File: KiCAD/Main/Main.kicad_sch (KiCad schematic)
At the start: 5 parts, among them J5 Conn_02x04_Counter_Clockwise

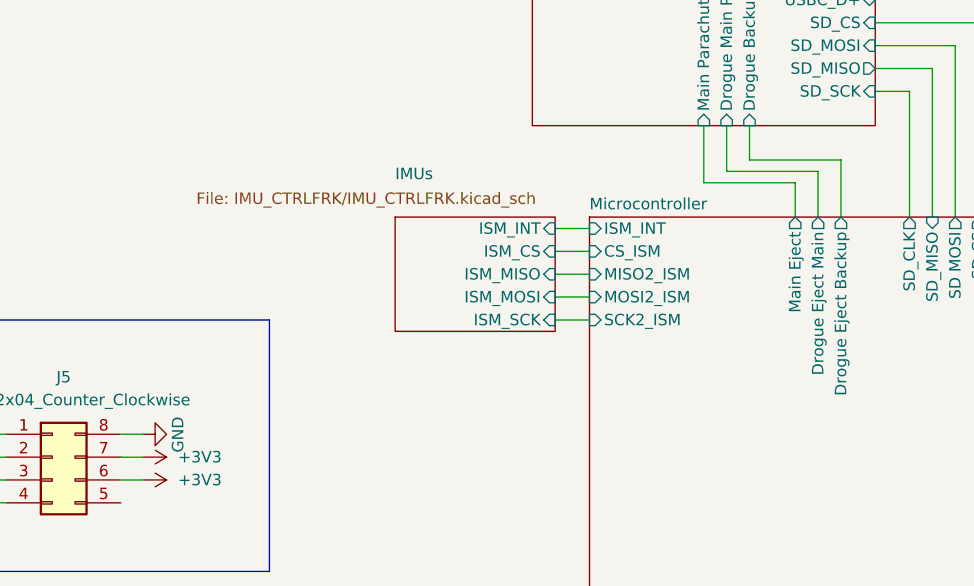
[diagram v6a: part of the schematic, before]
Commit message: Replace independent magnetometer, reformat test points, generate test gerber and BOM
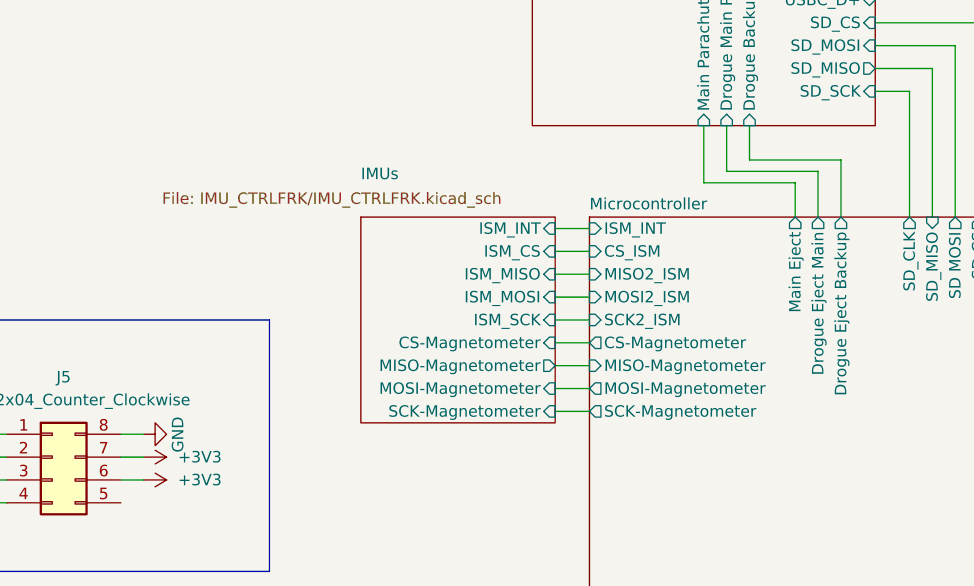
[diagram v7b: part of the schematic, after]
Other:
- sheet IMUs ports: added CS-Magnetometer, MISO-Magnetometer, MOSI-Magnetometer, SCK-Magnetometer; removed none
- sheet Microcontroller ports: added CS-Magnetometer, MISO-Magnetometer, MOSI-Magnetometer, SCK-Magnetometer; removed none
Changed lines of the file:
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@@
+	(wire
+		(pts
+			(xy 102.87 85.09) (xy 106.68 85.09)
+		)
+		(stroke
+			(width 0)
+			(type default)
+		)
+	)
 	(wire
 		(pts
@@
 	(wire
 		(pts
+			(xy 102.87 80.01) (xy 106.68 80.01)
+		)
+		(stroke
+			(width 0)
+			(type default)
+		)
+	)
+	(wire
+		(pts
 			(xy 168.91 113.03) (xy 172.72 113.03)
 		)
@@
 	(wire
 		(pts
+			(xy 102.87 82.55) (xy 106.68 82.55)
+		)
+		(stroke
+			(width 0)
+			(type default)
+		)
+	)
+	(wire
+		(pts
 			(xy 102.87 74.93) (xy 106.68 74.93)
 		)
@@
 		(pts
 			(xy 102.87 140.97) (xy 106.68 140.97)
+		)
+		(stroke
+			(width 0)
+			(type default)
+		)
+	)
+	(wire
+		(pts
+			(xy 102.87 87.63) (xy 106.68 87.63)
 		)
 		(stroke
@@
 			)
 		)
+		(pin "CS-Magnetometer" output
+			(at 106.68 80.01 180)
+			(effects
+				(font
+					(size 1.27 1.27)
+				)
+				(justify left)
+			)
+		)
+		(pin "MISO-Magnetometer" input
+			(at 106.68 82.55 180)
+			(effects
+				(font
+					(size 1.27 1.27)
+				)
+				(justify left)
+			)
+		)
+		(pin "MOSI-Magnetometer" output
+			(at 106.68 85.09 180)
+			(effects
+				(font
+					(size 1.27 1.27)
+				)
+				(justify left)
+			)
+		)
+		(pin "SCK-Magnetometer" output
+			(at 106.68 87.63 180)
+			(effects
+				(font
+					(size 1.27 1.27)
+				)
+				(justify left)
+			)
+		)
 		(instances
 			(project "Main"
@@
 	)
 	(sheet
-		(at 85.09 66.04)
-		(size 17.78 12.7)
+		(at 81.28 66.04)
+		(size 21.59 22.86)
 		(exclude_from_sim no)
 		(in_bom yes)
@@
 		)
 		(property "Sheetname" "IMUs"
-			(at 85.09 61.976 0)
+			(at 81.28 61.976 0)
 			(effects
 				(font
@@
 		)
 		(property "Sheetfile" "IMU_CTRLFRK/IMU_CTRLFRK.kicad_sch"
-			(at 62.992 63.246 0)
+			(at 59.182 63.246 0)
 			(effects
 				(font
@@
 			(effects
 				(font
+					(size 1.27 1.27)
+				)
+				(justify right)
+			)
+		)
+		(pin "CS-Magnetometer" input
+			(at 102.87 80.01 0)
+			(effects
+				(font
+					(size 1.27 1.27)
+				)
+				(justify right)
+			)
+		)
+		(pin "MISO-Magnetometer" output
+			(at 102.87 82.55 0)
+			(effects
+				(font
+					(size 1.27 1.27)
+				)
+				(justify right)
+			)
+		)
+		(pin "MOSI-Magnetometer" input
+			(at 102.87 85.09 0)
+			(effects
+				(font
+					(size 1.27 1.27)
+				)
+				(justify right)
+			)
+		)
+		(pin "SCK-Magnetometer" input
+			(at 102.87 87.63 0)
+			(effects
+				(font

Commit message: Update BOM and respective components according to LCSC supply, remove previously generated production files
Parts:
- J5: now left out of the parts list
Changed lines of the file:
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@@
 		(unit 1)
 		(exclude_from_sim no)
-		(in_bom yes)
+		(in_bom no)
 		(on_board yes)
 		(dnp no)
